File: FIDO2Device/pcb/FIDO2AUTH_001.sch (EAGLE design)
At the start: 25 parts, among them CN1 TE-1734028, SW1 SKRPACE010, SW2 SKTADAE010, U1 MDBT50Q-P1M, X1 NX3215SA-32.768K

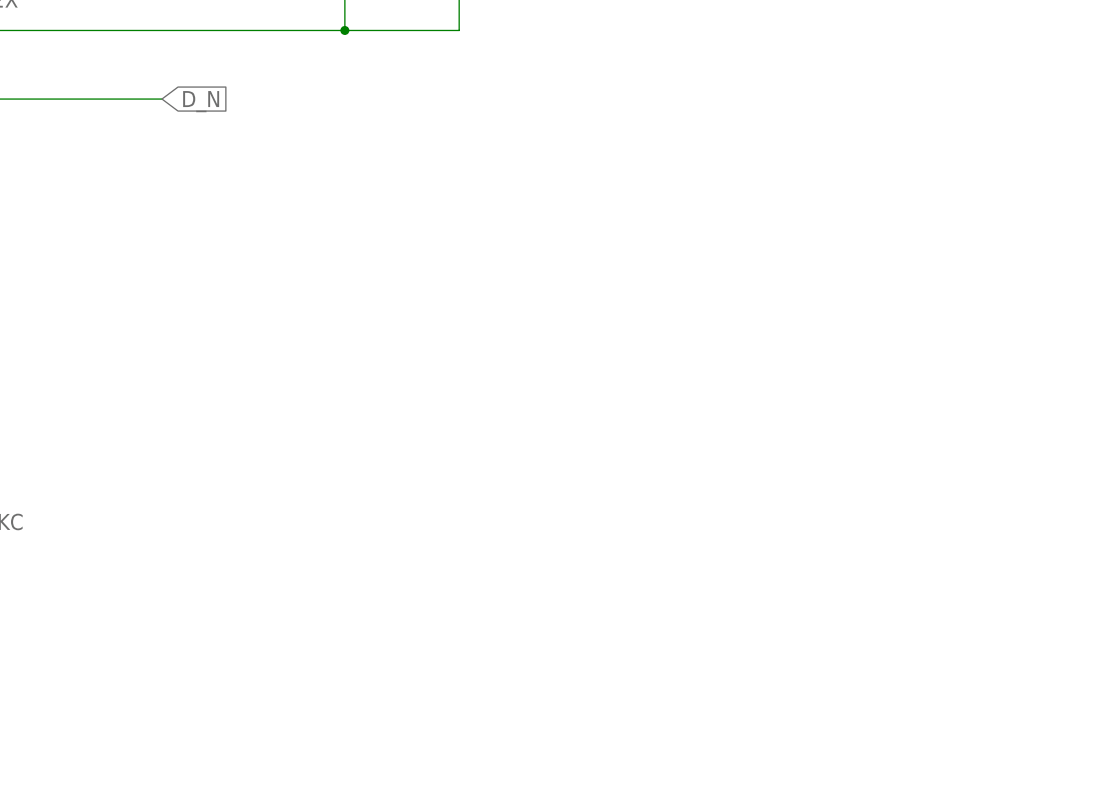
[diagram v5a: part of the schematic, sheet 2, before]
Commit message: [WIP] ブレークアウト基板回路図
・プログラミング・インターフェース（5Pスルーホール）配置
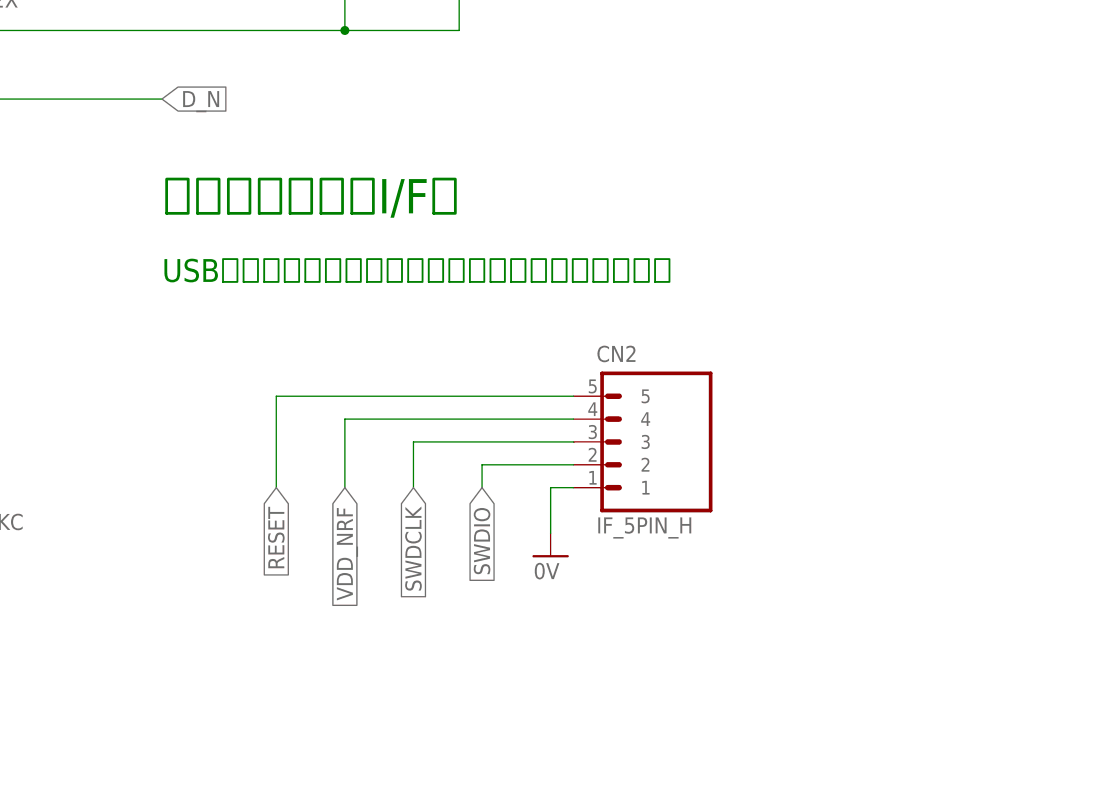
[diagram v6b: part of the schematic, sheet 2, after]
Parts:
- added CN2: IF_5PIN_H, Connectors:IF_5PIN_H
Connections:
- net 0V: now also CN2.1
- net RESET: now also CN2.5
- net SWDCLK: now also CN2.3
- net SWDIO: now also CN2.2
- net VDD_NRF: now also CN2.4
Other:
- note added: "USBブートローダーを初期書込する際に使用します。"
- note added: "プログラミングI/F部"
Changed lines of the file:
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@@
 <setting verticaltext="up"/>
 </settings>
-<grid distance="0.1" unitdist="inch" unit="inch" style="lines" multiple="1" display="yes" altdistance="0.01" altunitdist="inch" altunit="inch"/>
+<grid distance="0.1" unitdist="inch" unit="inch" style="lines" multiple="1" display="no" altdistance="0.01" altunitdist="inch" altunit="inch"/>
 <layers>
 <layer number="1" name="Top" color="4" fill="1" visible="no" active="no"/>
@@
 <part name="R4" library="Parts" deviceset="RESISTOR" device="_0402" value="2.2k"/>
 <part name="R5" library="Parts" deviceset="RESISTOR" device="_0402" value="390"/>
+<part name="CN2" library="Connectors" deviceset="IF_5PIN" device="_H"/>
+<part name="GND14" library="Supply" deviceset="0V" device=""/>
 </parts>
 <sheets>
@@
 開発用ブレークアウト基板</text>
 <text x="30.48" y="91.44" size="3.81" layer="91">LED部</text>
+<text x="147.32" y="91.44" size="3.81" layer="91">プログラミングI/F部</text>
+<text x="147.32" y="83.82" size="2.54" layer="91">USBブートローダーを初期書込する際に使用します。</text>
 </plain>
 <instances>
@@
 <instance part="R4" gate="G$1" x="96.52" y="40.64" rot="R90"/>
 <instance part="R5" gate="G$1" x="106.68" y="40.64" rot="R90"/>
+<instance part="CN2" gate="G$1" x="193.04" y="71.12"/>
+<instance part="GND14" gate="1" x="190.5" y="53.34"/>
 </instances>
 <busses>
@@
 <junction x="167.64" y="111.76"/>
 </segment>
+<segment>
+<pinref part="GND14" gate="1" pin="0V"/>
+<wire x1="190.5" y1="55.88" x2="190.5" y2="60.96" width="0.1524" layer="91"/>
+<pinref part="CN2" gate="G$1" pin="1"/>
+<wire x1="190.5" y1="60.96" x2="193.04" y2="60.96" width="0.1524" layer="91"/>
+</segment>
 </net>
 <net name="N$2" class="0">
@@
 <label x="91.44" y="68.58" size="1.778" layer="95" rot="R90" xref="yes"/>
 </segment>
+<segment>
+<pinref part="CN2" gate="G$1" pin="4"/>
+<wire x1="193.04" y1="68.58" x2="167.64" y2="68.58" width="0.1524" layer="91"/>
+<wire x1="167.64" y1="68.58" x2="167.64" y2="60.96" width="0.1524" layer="91"/>
+<label x="167.64" y="60.96" size="1.778" layer="95" rot="R270" xref="yes"/>
+</segment>
 </net>
 <net name="LED1" class="0">
@@
 </segment>
 </net>
+<net name="SWDIO" class="0">
+<segment>
+<pinref part="CN2" gate="G$1" pin="2"/>
+<wire x1="193.04" y1="63.5" x2="182.88" y2="63.5" width="0.1524" layer="91"/>
+<wire x1="182.88" y1="63.5" x2="182.88" y2="60.96" width="0.1524" layer="91"/>
+<label x="182.88" y="60.96" size="1.778" layer="95" rot="R270" xref="yes"/>
+</segment>
+</net>
+<net name="SWDCLK" class="0">
+<segment>
+<pinref part="CN2" gate="G$1" pin="3"/>
+<wire x1="193.04" y1="66.04" x2="175.26" y2="66.04" width="0.1524" layer="91"/>
+<wire x1="175.26" y1="66.04" x2="175.26" y2="60.96" width="0.1524" layer="91"/>
+<label x="175.26" y="60.96" size="1.778" layer="95" rot="R270" xref="yes"/>
+</segment>
+</net>
+<net name="RESET" class="0">
+<segment>
+<pinref part="CN2" gate="G$1" pin="5"/>
+<wire x1="193.04" y1="71.12" x2="160.02" y2="71.12" width="0.1524" layer="91"/>
+<wire x1="160.02" y1="71.12" x2="160.02" y2="60.96" width="0.1524" layer="91"/>
+<label x="160.02" y="60.96" size="1.778" layer="95" rot="R270" xref="yes"/>
+</segment>
+</net>

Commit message: [WIP] ブレークアウト基板回路図
・電源供給回路を追加
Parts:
- added C10, C11: 1uF, Parts:CAP_0603
- added D2, D3: PMEG2005AEA,115, Parts:PMEG2005AEA,115
- added U2: XC6206P332MR-G, Parts:XC6206P332MR-G
- C5: value 10uF -> 0.01uF
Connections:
- new net N$4: C11.1, D2.A, U2.VOUT
- net 0V: now also C10.2, C11.2, U2.VSS
- net VBUS_NRF: now also C10.1, U2.VIN
- net VDD_NRF: now also D2.C, D3.C
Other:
- note added: "USBポートに装着時は、VBUSの5.0V-->3.3Vに降圧して供給します。 乾電池ホルダーにボタン乾電池を装着した場合は、3.0Vを供給します。"
- note added: "ここにボタン乾電池ケースを 追加します。"
- note added: "電源供給部"
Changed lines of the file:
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@@
 <setting verticaltext="up"/>
 </settings>
-<grid distance="0.1" unitdist="inch" unit="inch" style="lines" multiple="1" display="no" altdistance="0.01" altunitdist="inch" altunit="inch"/>
+<grid distance="0.1" unitdist="inch" unit="inch" style="lines" multiple="1" display="yes" altdistance="0.01" altunitdist="inch" altunit="inch"/>
 <layers>
 <layer number="1" name="Top" color="4" fill="1" visible="no" active="no"/>
@@
 <part name="FB1" library="Parts" deviceset="BLM15AG" device="121SN1D"/>
 <part name="FB2" library="Parts" deviceset="BLM15AG" device="121SN1D"/>
-<part name="C5" library="Parts" deviceset="CAP" device="_0603" value="10uF"/>
+<part name="C5" library="Parts" deviceset="CAP" device="_0603" value="0.01uF"/>
 <part name="C6" library="Parts" deviceset="CAP" device="_0603" value="10uF"/>
 <part name="C7" library="Parts" deviceset="CAP" device="_0402" value="0.1uF"/>
@@
 <part name="CN2" library="Connectors" deviceset="IF_5PIN" device="_H"/>
 <part name="GND14" library="Supply" deviceset="0V" device=""/>
+<part name="FRAME3" library="Generic" deviceset="A4L-LOC" device=""/>
+<part name="U2" library="Parts" deviceset="XC6206" device="P332MR-G"/>
+<part name="C10" library="Parts" deviceset="CAP" device="_0603" value="1uF"/>
+<part name="C11" library="Parts" deviceset="CAP" device="_0603" value="1uF"/>
+<part name="GND15" library="Supply" deviceset="0V" device=""/>
+<part name="GND16" library="Supply" deviceset="0V" device=""/>
+<part name="GND17" library="Supply" deviceset="0V" device=""/>
+<part name="D2" library="Parts" deviceset="PMEG2005" device="AEA,115"/>
+<part name="D3" library="Parts" deviceset="PMEG2005" device="AEA,115"/>
 </parts>
 <sheets>
@@
 <pinref part="C7" gate="G$1" pin="1"/>
 <wire x1="104.14" y1="157.48" x2="104.14" y2="154.94" width="0.1524" layer="91"/>
-<wire x1="104.14" y1="157.48" x2="109.22" y2="157.48" width="0.1524" layer="91"/>
+<wire x1="104.14" y1="157.48" x2="119.38" y2="157.48" width="0.1524" layer="91"/>
 <junction x="104.14" y="157.48"/>
-<label x="109.22" y="157.48" size="1.778" layer="95" xref="yes"/>
+<label x="119.38" y="157.48" size="1.778" layer="95" xref="yes"/>
 </segment>
 </net>
@@
 </segment>
 </net>
+</nets>
+</sheet>
+<sheet>
+<plain>
+<text x="218.44" y="20.32" size="1.778" layer="91">MDBT50Q-P1M Breakout</text>
+<text x="166.37" y="11.43" size="2.54" layer="91">nRF52840版FIDO2認証器
+開発用ブレークアウト基板</text>
+<text x="35.56" y="152.4" size="3.81" layer="91">電源供給部</text>
+<text x="35.56" y="147.32" size="2.54" layer="91" align="top-left">USBポートに装着時は、VBUSの5.0V--&gt;3.3Vに降圧して供給します。
+乾電池ホルダーにボタン乾電池を装着した場合は、3.0Vを供給します。</text>
+<text x="66.04" y="76.2" size="2.54" layer="91">ここにボタン乾電池ケースを
+追加します。</text>
+</plain>
+<instances>
+<instance part="FRAME3" gate="G$1" x="0" y="0"/>
+<instance part="U2" gate="G$1" x="73.66" y="124.46"/>
+<instance part="C10" gate="G$1" x="66.04" y="116.84"/>
+<instance part="C11" gate="G$1" x="111.76" y="116.84"/>
+<instance part="GND15" gate="1" x="101.6" y="101.6"/>
+<instance part="GND16" gate="1" x="66.04" y="101.6"/>
+<instance part="GND17" gate="1" x="111.76" y="101.6"/>
+<instance part="D2" gate="G$1" x="121.92" y="124.46"/>
+<instance part="D3" gate="G$1" x="121.92" y="81.28"/>
+</instances>
+<busses>
+</busses>
+<nets>
+<net name="0V" class="0">
+<segment>
+<pinref part="C10" gate="G$1" pin="2"/>
+<pinref part="GND16" gate="1" pin="0V"/>
+<wire x1="66.04" y1="109.22" x2="66.04" y2="104.14" width="0.1524" layer="91"/>
+</segment>
+<segment>
+<pinref part="U2" gate="G$1" pin="VSS"/>
+<pinref part="GND15" gate="1" pin="0V"/>
+<wire x1="96.52" y1="119.38" x2="101.6" y2="119.38" width="0.1524" layer="91"/>
+<wire x1="101.6" y1="119.38" x2="101.6" y2="104.14" width="0.1524" layer="91"/>
+</segment>
+<segment>
+<pinref part="C11" gate="G$1" pin="2"/>
+<pinref part="GND17" gate="1" pin="0V"/>
+<wire x1="111.76" y1="109.22" x2="111.76" y2="104.14" width="0.1524" layer="91"/>
+</segment>
+</net>
+<net name="N$4" class="0">
+<segment>
+<pinref part="U2" gate="G$1" pin="VOUT"/>
+<wire x1="96.52" y1="124.46" x2="111.76" y2="124.46" width="0.1524" layer="91"/>
+<pinref part="C11" gate="G$1" pin="1"/>
+<wire x1="111.76" y1="124.46" x2="119.38" y2="124.46" width="0.1524" layer="91"/>
+<wire x1="111.76" y1="124.46" x2="111.76" y2="116.84" width="0.1524" layer="91"/>
+<junction x="111.76" y="124.46"/>
+<pinref part="D2" gate="G$1" pin="A"/>
+</segment>
+</net>
+<net name="VBUS_NRF" class="0">
+<segment>
+<pinref part="U2" gate="G$1" pin="VIN"/>
+<pinref part="C10" gate="G$1" pin="1"/>
+<wire x1="73.66" y1="121.92" x2="66.04" y2="121.92" width="0.1524" layer="91"/>
+<wire x1="66.04" y1="121.92" x2="66.04" y2="116.84" width="0.1524" layer="91"/>
+<wire x1="66.04" y1="121.92" x2="58.42" y2="121.92" width="0.1524" layer="91"/>
+<junction x="66.04" y="121.92"/>
+<label x="58.42" y="121.92" size="1.778" layer="95" rot="R180" xref="yes"/>
+</segment>
+</net>
+<net name="VDD_NRF" class="0">
+<segment>
+<wire x1="124.46" y1="124.46" x2="144.78" y2="124.46" width="0.1524" layer="91"/>
+<label x="149.86" y="124.46" size="1.778" layer="95" xref="yes"/>
+<pinref part="D2" gate="G$1" pin="C"/>
+<pinref part="D3" gate="G$1" pin="C"/>
+<wire x1="144.78" y1="124.46" x2="149.86" y2="124.46" width="0.1524" layer="91"/>
+<wire x1="124.46" y1="81.28" x2="144.78" y2="81.28" width="0.1524" layer="91"/>
+<wire x1="144.78" y1="81.28" x2="144.78" y2="124.46" width="0.1524" layer="91"/>
+<junction x="144.78" y="124.46"/>
+</segment>
+</net>
+<net name="N$1" class="0">
+<segment>
+<wire x1="63.5" y1="88.9" x2="114.3" y2="88.9" width="0.1524" layer="91"/>
+<wire x1="114.3" y1="88.9" x2="114.3" y2="71.12" width="0.1524" layer="91"/>
+<wire x1="114.3" y1="71.12" x2="63.5" y2="71.12" width="0.1524" layer="91"/>
+<wire x1="63.5" y1="71.12" x2="63.5" y2="88.9" width="0.1524" layer="91"/>
+</segment>
+</net>
